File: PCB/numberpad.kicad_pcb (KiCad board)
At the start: 2 copper layers, 97 x 124.9 mm, 57 parts, among them J1 Light_Sensor, J2 Rotary_Encoder, J3 Screen_Connector, J4 FingerPrint, SW0 0, SW1 ., SW10 8, SW11 9, SW12 +, SW13 num_lock, SW14 /, SW15 *, SW16 -, SW2 1, SW3 2, SW4 3, SW5 enter, SW6 4, SW7 5, SW8 6, SW9 7, U1 ATmega328-P, U2 ESP32-S3-DEVKITC-1-N8R2

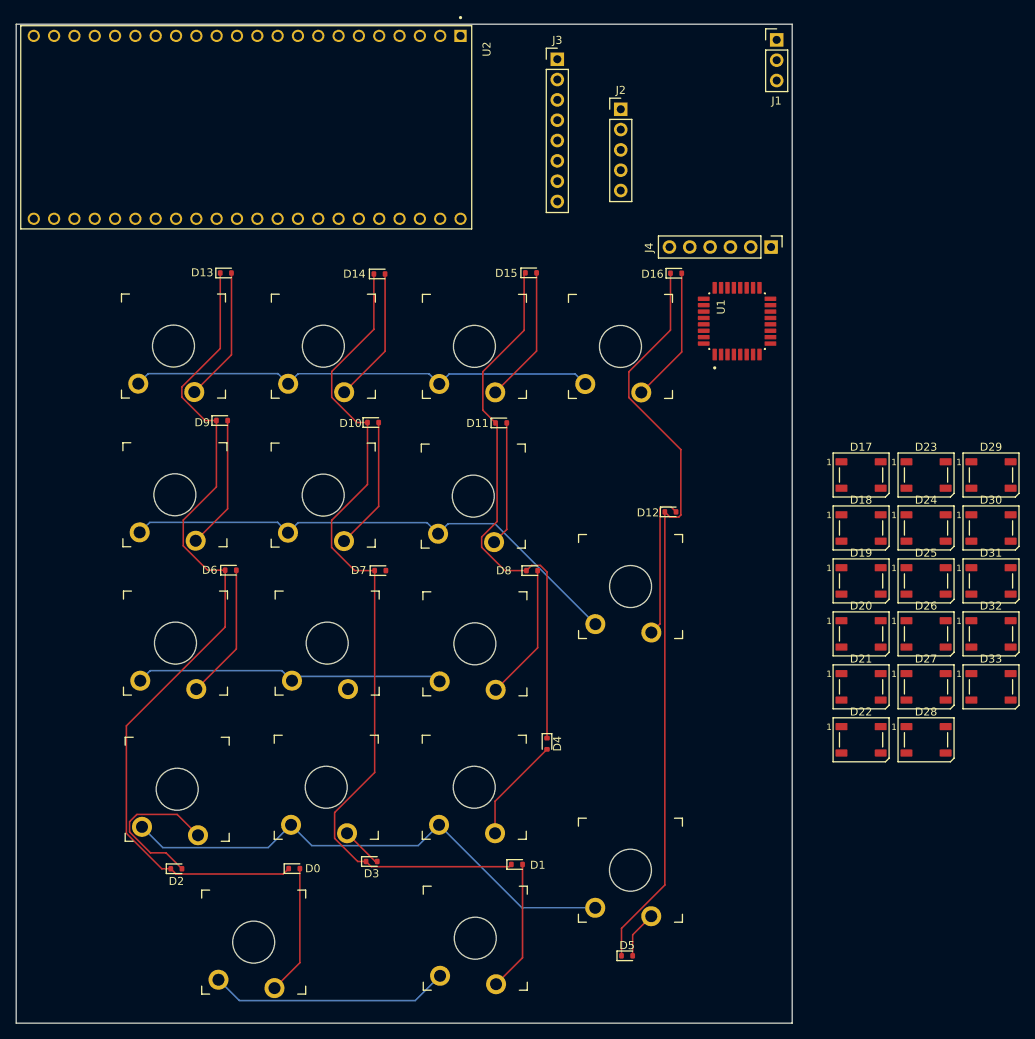
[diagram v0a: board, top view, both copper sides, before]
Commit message: Windows support !
Windows HID support have been added in this version also working with Android. Both only work with default keymap.
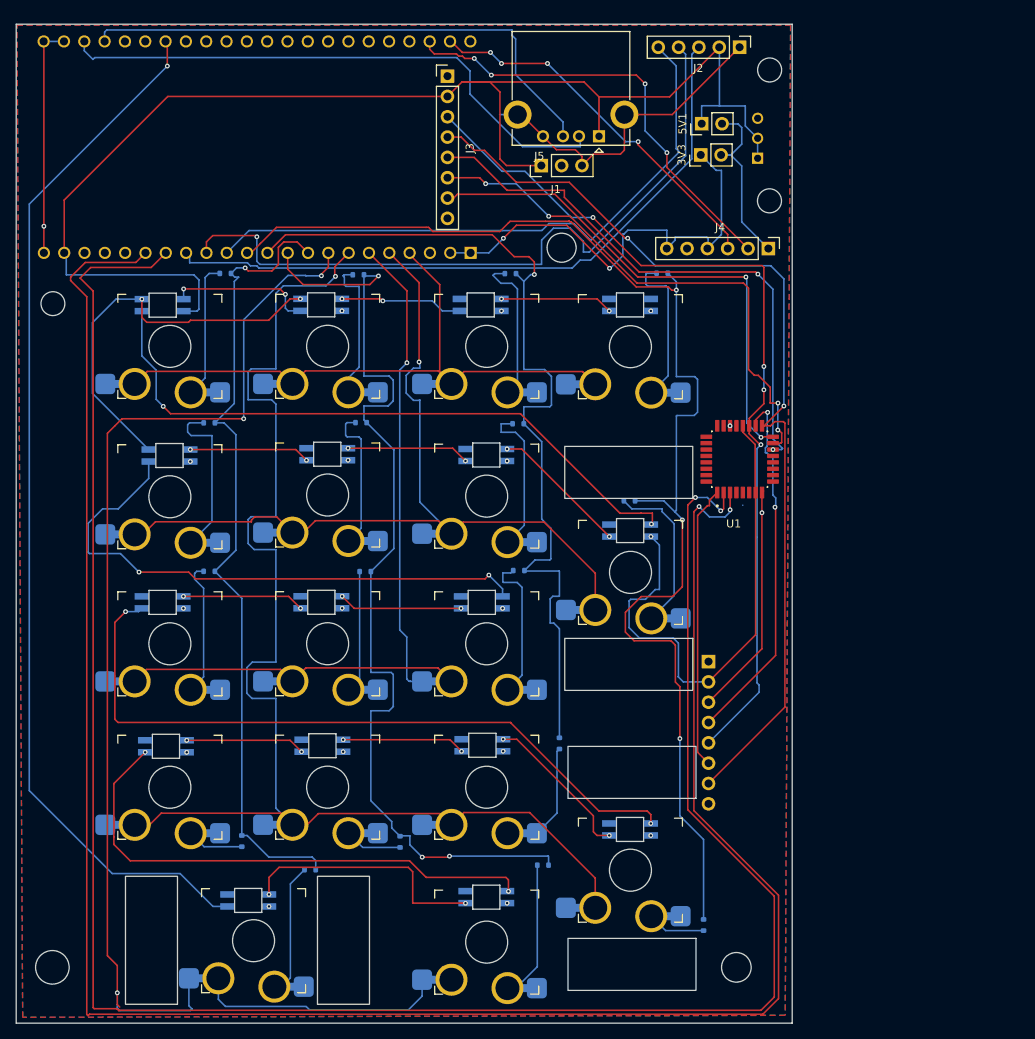
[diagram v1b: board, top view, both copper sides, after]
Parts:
- added 3V3: Conn_01x02_Pin, Connector_PinHeader_2.54mm:PinHeader_1x02_P2.54mm_Vertical, F.Cu at (125.8, 57.2)
- added 5V1: Conn_01x02_Pin, Connector_PinHeader_2.54mm:PinHeader_1x02_P2.54mm_Vertical, F.Cu at (125.9, 53.3)
- added J5: USB_A, Connector_USB:USB_A_Kycon_KUSBX-AS1N-B_Horizontal, F.Cu at (113.0, 54.9)
- added J6: Programmer, Connector_PinSocket_2.54mm:PinSocket_1x08_P2.54mm_Horizontal, B.Cu at (126.7, 120.5)
- added REF**: 2U Stabilizer, footprints:Gateron-KS33-2u-Stabilizer-Cutout, F.Cu at (115.4, 146.4)
- added REF**: 2U Stabilizer, footprints:Gateron-KS33-2u-Stabilizer-Cutout, F.Cu at (115.0, 108.9)
- added REF**: 2U Stabilizer, footprints:Gateron-KS33-2u-Stabilizer-Cutout, F.Cu at (69.1, 153.6)
- added S1: MINI-SPDT-SW, footprints:SW_MINI-SPDT-SW, B.Cu at (132.9, 55.1)
- D0, D1, D10, D11, D12, D13, D14, D15, D16, D2, D3, D4, D5, D6, D7, D8, D9: moved to B.Cu
- D17, D18, D19, D20, D21, D22, D23, D24, D25, D26, D27, D28, D29, D30, D31, D32, D33: value WS2812B -> SK6812MINI; footprint LED_SMD:LED_WS2812B_PLCC4_5.0x5.0mm_P3.2mm -> footprints:LED_SK6812-E; moved to B.Cu
- J4: value FingerPrint -> FingerPrint_UART
- SW0, SW1, SW10, SW11, SW12, SW13, SW14, SW15, SW16, SW2, SW3, SW4, SW5, SW6, SW7, SW8, SW9: footprint footprints:SW_Gateron_LowProfile_THT -> footprints:SW_Gateron_LowProfile_HotSwap_PTH
- U2: value ESP32-S3-DEVKITC-1-N8R2 -> ESP32-S3-DEVKITC-1-N16R8V; footprint footprints:ESP32-S3-DEVKITC-1-N8R8 -> footprints:XCVR_ESP32-S3-DEVKITC-1-N8R2; moved to B.Cu
- moved D30 107.2 mm to (58.5, 76.0)
- moved D26 97.2 mm to (59.4, 94.8)
- moved D23 96.7 mm to (58.5, 113.1)
- moved D17 93.3 mm to (69.2, 150.4)
- moved D31 90.6 mm to (78.3, 76.0)
- moved D19 89.3 mm to (58.9, 131.1)
- moved D27 80.3 mm to (79.1, 94.6)
- moved D24 76.2 mm to (78.3, 113.1)
- moved D32 75.9 mm to (98.2, 76.0)
- moved D20 68.8 mm to (78.5, 131.1)
- moved D18 65.8 mm to (99.0, 150.0)
- moved D33 65.7 mm to (116.9, 76.0)
- moved D28 65.5 mm to (99.0, 94.7)
- moved D25 55.6 mm to (98.4, 113.1)
- moved D21 47.9 mm to (98.5, 131.0)
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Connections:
- net SCREEN_SCL_SCK renamed PB5
- net SCREEN_SDA_MOSI renamed PB3
- D17 pad 1: unconnected-(D17-VDD-Pad1) -> 5V
- D17 pad 2: unconnected-(D17-DOUT-Pad2) -> Net-(D17-DOUT)
- D17 pad 3: unconnected-(D17-VSS-Pad3) -> GND
- D17 pad 4: unconnected-(D17-DIN-Pad4) -> LEDS_Out
- D18 pad 1: unconnected-(D18-VDD-Pad1) -> 5V
- D18 pad 2: unconnected-(D18-DOUT-Pad2) -> R0_LED
- D18 pad 3: unconnected-(D18-VSS-Pad3) -> GND
- D18 pad 4: unconnected-(D18-DIN-Pad4) -> Net-(D17-DOUT)
- D19 pad 1: unconnected-(D19-VDD-Pad1) -> 5V
- D19 pad 2: unconnected-(D19-DOUT-Pad2) -> Net-(D19-DOUT)
- D19 pad 3: unconnected-(D19-VSS-Pad3) -> GND
- D19 pad 4: unconnected-(D19-DIN-Pad4) -> R0_LED
- D20 pad 1: unconnected-(D20-VDD-Pad1) -> 5V
- D20 pad 2: unconnected-(D20-DOUT-Pad2) -> Net-(D20-DOUT)
- D20 pad 3: unconnected-(D20-VSS-Pad3) -> GND
- D20 pad 4: unconnected-(D20-DIN-Pad4) -> Net-(D19-DOUT)
- D21 pad 1: unconnected-(D21-VDD-Pad1) -> 5V
- D21 pad 2: unconnected-(D21-DOUT-Pad2) -> Net-(D21-DOUT)
- D21 pad 3: unconnected-(D21-VSS-Pad3) -> GND
- D21 pad 4: unconnected-(D21-DIN-Pad4) -> Net-(D20-DOUT)
- D22 pad 1: unconnected-(D22-VDD-Pad1) -> 5V
- D22 pad 2: unconnected-(D22-DOUT-Pad2) -> R1_LED
- D22 pad 3: unconnected-(D22-VSS-Pad3) -> GND
- D22 pad 4: unconnected-(D22-DIN-Pad4) -> Net-(D21-DOUT)
- D23 pad 1: unconnected-(D23-VDD-Pad1) -> 5V
- D23 pad 2: unconnected-(D23-DOUT-Pad2) -> Net-(D23-DOUT)
- D23 pad 3: unconnected-(D23-VSS-Pad3) -> GND
- D23 pad 4: unconnected-(D23-DIN-Pad4) -> R1_LED
- D24 pad 1: unconnected-(D24-VDD-Pad1) -> 5V
- D24 pad 2: unconnected-(D24-DOUT-Pad2) -> Net-(D24-DOUT)
- D24 pad 3: unconnected-(D24-VSS-Pad3) -> GND
- D24 pad 4: unconnected-(D24-DIN-Pad4) -> Net-(D23-DOUT)
- D25 pad 1: unconnected-(D25-VDD-Pad1) -> 5V
- D25 pad 2: unconnected-(D25-DOUT-Pad2) -> R2_LED
- D25 pad 3: unconnected-(D25-VSS-Pad3) -> GND
- D25 pad 4: unconnected-(D25-DIN-Pad4) -> Net-(D24-DOUT)
- D26 pad 1: unconnected-(D26-VDD-Pad1) -> 5V
- D26 pad 2: unconnected-(D26-DOUT-Pad2) -> Net-(D26-DOUT)
- D26 pad 3: unconnected-(D26-VSS-Pad3) -> GND
- D26 pad 4: unconnected-(D26-DIN-Pad4) -> R2_LED
- D27 pad 1: unconnected-(D27-VDD-Pad1) -> 5V
- D27 pad 2: unconnected-(D27-DOUT-Pad2) -> Net-(D27-DOUT)
- D27 pad 3: unconnected-(D27-VSS-Pad3) -> GND
- D27 pad 4: unconnected-(D27-DIN-Pad4) -> Net-(D26-DOUT)
- D28 pad 1: unconnected-(D28-VDD-Pad1) -> 5V
- D28 pad 2: unconnected-(D28-DOUT-Pad2) -> Net-(D28-DOUT)
- D28 pad 3: unconnected-(D28-VSS-Pad3) -> GND
- D28 pad 4: unconnected-(D28-DIN-Pad4) -> Net-(D27-DOUT)
- D29 pad 1: unconnected-(D29-VDD-Pad1) -> 5V
- D29 pad 2: unconnected-(D29-DOUT-Pad2) -> R3_LED
- D29 pad 3: unconnected-(D29-VSS-Pad3) -> GND
- D29 pad 4: unconnected-(D29-DIN-Pad4) -> Net-(D28-DOUT)
- D30 pad 1: unconnected-(D30-VDD-Pad1) -> 5V
- D30 pad 2: unconnected-(D30-DOUT-Pad2) -> Net-(D30-DOUT)
- D30 pad 3: unconnected-(D30-VSS-Pad3) -> GND
- D30 pad 4: unconnected-(D30-DIN-Pad4) -> R3_LED
- D31 pad 1: unconnected-(D31-VDD-Pad1) -> 5V
- D31 pad 2: unconnected-(D31-DOUT-Pad2) -> Net-(D31-DOUT)
- D31 pad 3: unconnected-(D31-VSS-Pad3) -> GND
- D31 pad 4: unconnected-(D31-DIN-Pad4) -> Net-(D30-DOUT)
- D32 pad 1: unconnected-(D32-VDD-Pad1) -> 5V
- D32 pad 2: unconnected-(D32-DOUT-Pad2) -> Net-(D32-DOUT)
- D32 pad 3: unconnected-(D32-VSS-Pad3) -> GND
- D32 pad 4: unconnected-(D32-DIN-Pad4) -> Net-(D31-DOUT)
- D33 pad 1: unconnected-(D33-VDD-Pad1) -> 5V
- D33 pad 3: unconnected-(D33-VSS-Pad3) -> GND
- D33 pad 4: unconnected-(D33-DIN-Pad4) -> Net-(D32-DOUT)
- J1 pad 1: +5V -> 5V
- J1 pad 2: Light_out -> Light_int
- J2 pad 2: +5V -> 5V
- J3 pad 2: +5V -> 5V
- J4 pad 4: +3.3V -> 3V3
- J4 pad 6: +3.3V -> 3V3
- U1 pad 1: unconnected-(U1-~{RESET}/PC6-Pad1) -> PC6
- U1 pad 18: unconnected-(U1-PB4-Pad18) -> PB4
- U1 pad 20: +5V -> 5V
- U1 pad 23: Light_out -> Light_in
- U1 pad 7: +5V -> 5V
- U2 pad J1_1: +3V3 -> 3V3
- U2 pad J1_18: (no net) -> unconnected-(U2-GPIO12-PadJ1_18)
- U2 pad J1_19: (no net) -> unconnected-(U2-GPIO13-PadJ1_19)
- U2 pad J1_2: +3V3 -> 3V3
- U2 pad J1_20: (no net) -> unconnected-(U2-GPIO14-PadJ1_20)
- U2 pad J1_21: +5V -> 5V
- U2 pad J1_3: unconnected-(U2-RST-PadJ1_3) -> RST
- U2 pad J3_10: (no net) -> unconnected-(U2-GPIO38-PadJ3_10)
- U2 pad J3_11: (no net) -> unconnected-(U2-GPIO37-PadJ3_11)
- U2 pad J3_12: (no net) -> unconnected-(U2-GPIO36-PadJ3_12)
- U2 pad J3_13: (no net) -> unconnected-(U2-GPIO35-PadJ3_13)
- U2 pad J3_15: (no net) -> unconnected-(U2-GPIO45-PadJ3_15)
- U2 pad J3_16: (no net) -> LEDS_Out
- U2 pad J3_17: (no net) -> unconnected-(U2-GPIO47-PadJ3_17)
- U2 pad J3_18: (no net) -> unconnected-(U2-GPIO21-PadJ3_18)
- U2 pad J3_19: (no net) -> D+
- U2 pad J3_2: (no net) -> TX2
- U2 pad J3_20: (no net) -> D-
- U2 pad J3_3: (no net) -> RX2
- U2 pad J3_6: (no net) -> unconnected-(U2-MTMS/GPIO42-PadJ3_6)
- U2 pad J3_7: (no net) -> unconnected-(U2-MTDI/GPIO41-PadJ3_7)
- U2 pad J3_8: (no net) -> unconnected-(U2-MTDO/GPIO40-PadJ3_8)
- U2 pad J3_9: (no net) -> unconnected-(U2-MTCK/GPIO39-PadJ3_9)
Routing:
- net TX: track 0.00 -> 264.3 mm, vias 0 -> 2
- net RX: track 0.00 -> 263.6 mm, vias 0 -> 2
- net 5V: track 0.00 -> 235.4 mm, vias 0 -> 16
- net GND: track 0.00 -> 172.8 mm, vias 0 -> 5
- net R4: track 30.1 -> 166.3 mm, vias 0 -> 3
- net LEDS_Out: track 0.00 -> 131.6 mm, vias 0 -> 1
- net PB3: track 0.00 -> 121.2 mm, vias 0 -> 2
- net PB5: track 0.00 -> 111.2 mm, vias 0 -> 4
- net R3: track 65.4 -> 166.2 mm, vias 0 -> 1
- net DT: track 0.00 -> 89.4 mm, vias 0 -> 1
- net R1_LED: track 0.00 -> 89.3 mm, vias 0 -> 2
- net SW: track 0.00 -> 84.4 mm
- net R3_LED: track 0.00 -> 81.1 mm, vias 0 -> 2
- net CLK: track 0.00 -> 77.7 mm
- net D-: track 0.00 -> 71.4 mm
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- added copper zone on F.Cu, net 5V
- added copper zone on B.Cu, net GND
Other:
- outline, holes or cut-outs redrawn

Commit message: update to support volume on android + update screen. missing device connected name + last key pressed
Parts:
- added C1: 100nF, Capacitor_THT:C_Rect_L4.6mm_W2.0mm_P2.50mm_MKS02_FKP02, F.Cu at (76.4, 52.9)
- added C2: 100nF, Capacitor_THT:C_Rect_L4.6mm_W2.0mm_P2.50mm_MKS02_FKP02, F.Cu at (84.5, 52.8)
- added J7: USB_C_TO_PC, Connector_PinHeader_1.00mm:PinHeader_1x04_P1.00mm_Vertical, F.Cu at (42.4, 55.3)
- added R1: 10K, Resistor_THT:R_Axial_DIN0204_L3.6mm_D1.6mm_P7.62mm_Horizontal, F.Cu at (73.6, 58.5)
- added R2: 12K1, Resistor_THT:R_Axial_DIN0204_L3.6mm_D1.6mm_P7.62mm_Horizontal, F.Cu at (73.7, 63.8)
- added U3: USB2514B_Bi, Package_DFN_QFN:QFN-36-1EP_6x6mm_P0.5mm_EP3.7x3.7mm, F.Cu at (66.2, 61.3)
- added Y1: Crystal_Small, footprints:XTAL_HC49P488W43L1150T466H350, F.Cu at (66.3, 53.2)
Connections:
- J5 pad 2: D- -> DS-
- J5 pad 3: D+ -> DS+
- U2 pad J3_19: D+ -> DE+
- U2 pad J3_20: D- -> DE-
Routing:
- net DS+: track 0.00 -> 82.9 mm, vias 0 -> 1
- net DS-: track 0.00 -> 74.4 mm, vias 0 -> 1
- net Net-(U3-RBIAS): track 0.00 -> 34.8 mm, vias 0 -> 1
- net Net-(U3-CRFILT): track 0.00 -> 31.2 mm
- net D+: track 68.1 -> 39.4 mm, vias 0 -> 2
- net D-: track 71.4 -> 42.9 mm, vias 0 -> 2
- net DE-: track 0.00 -> 25.1 mm, vias 0 -> 2
- net DE+: track 0.00 -> 24.5 mm, vias 0 -> 2
- net Net-(U3-PLLFILT): track 0.00 -> 22.9 mm
- net +3.3V: track 0.00 -> 22.6 mm, vias 0 -> 1
- net Net-(U3-XTALOUT): track 0.00 -> 14.8 mm
- net Net-(U3-RESET_N): track 0.00 -> 13.5 mm
- net Net-(U3-XTALIN/CLKIN): track 0.00 -> 6.44 mm
- net GND: track 172.8 -> 172.9 mm, vias 5 -> 7
